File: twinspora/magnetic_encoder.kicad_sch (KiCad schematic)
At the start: 7 parts, among them J8 XY-SH1_0-6A51, U10 SRV05-4A, U8 MT6701QT

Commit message: NEW
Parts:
- C33: footprint Basic_Capacitors_Resistors:C0402 -> Capacitor_SMD:C_0402_1005Metric
- R26, R28, R30: footprint Basic_Capacitors_Resistors:R0603 -> Resistor_SMD:R_0603_1608Metric
- U10: footprint Package_TO_SOT_SMD:SOT-23-6 -> lemon-pepper-footprints:SOT-23-6
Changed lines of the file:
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@@
 		)
 	)
-	(text_box "SH breakouts for remote motor encoder connection (Must remove existing sensor)"
+	(text_box "SH breakouts for remote motor encoder connection (Desolder 0603 0Ω resistors)"
 		(exclude_from_sim no)
-		(at 182.88 66.04 0)
-		(size 26.67 13.3968)
+		(at 181.61 70.4232 0)
+		(size 24.13 9.5868)
 		(margins 0.9525 0.9525 0.9525 0.9525)
 		(stroke
@@
 		(dnp no)
 		(fields_autoplaced yes)
-		(property "Reference" "#PWR075"
+		(property "Reference" "#PWR75"
 			(at 173.99 81.28 0)
 			(hide yes)
@@
 			(project "twinspora"
 				(path "/64e594d2-0aaa-4fb1-a4b5-254d61e53018/0c28785f-fbfa-498f-abec-3f4cc9ccf6c4"
-					(reference "#PWR076")
+					(reference "#PWR76")
 					(unit 1)
 				)
 				(path "/64e594d2-0aaa-4fb1-a4b5-254d61e53018/59ac2ac7-da91-4c77-8dbc-3d7c7b498637"
-					(reference "#PWR075")
+					(reference "#PWR75")
 					(unit 1)
 				)
@@
 			)
 		)
-		(property "Footprint" "Basic_Capacitors_Resistors:R0603"
+		(property "Footprint" "Resistor_SMD:R_0603_1608Metric"
 			(at 115.57 102.87 0)
 			(hide yes)
@@
 		(dnp no)
 		(fields_autoplaced yes)
-		(property "Reference" "#PWR073"
+		(property "Reference" "#PWR73"
 			(at 215.9 81.28 0)
 			(hide yes)
@@
 			(project "twinspora"
 				(path "/64e594d2-0aaa-4fb1-a4b5-254d61e53018/0c28785f-fbfa-498f-abec-3f4cc9ccf6c4"
-					(reference "#PWR078")
+					(reference "#PWR78")
 					(unit 1)
 				)
 				(path "/64e594d2-0aaa-4fb1-a4b5-254d61e53018/59ac2ac7-da91-4c77-8dbc-3d7c7b498637"
-					(reference "#PWR073")
+					(reference "#PWR73")
 					(unit 1)
 				)
@@
 		(dnp no)
 		(fields_autoplaced yes)
-		(property "Reference" "#PWR074"
+		(property "Reference" "#PWR74"
 			(at 176.53 130.81 0)
 			(hide yes)
@@
 			(project "twinspora"
 				(path "/64e594d2-0aaa-4fb1-a4b5-254d61e53018/0c28785f-fbfa-498f-abec-3f4cc9ccf6c4"
-					(reference "#PWR077")
+					(reference "#PWR77")
 					(unit 1)
 				)
 				(path "/64e594d2-0aaa-4fb1-a4b5-254d61e53018/59ac2ac7-da91-4c77-8dbc-3d7c7b498637"
-					(reference "#PWR074")
+					(reference "#PWR74")
 					(unit 1)
 				)
@@
 		(dnp no)
 		(property "Reference" "C33"
-			(at 152.654 110.49 0)
+			(at 156.21 110.49 0)
 			(show_name no)
 			(do_not_autoplace no)
@@
 			)
 		)
-		(property "Footprint" "Basic_Capacitors_Resistors:C0402"
+		(property "Footprint" "Capacitor_SMD:C_0402_1005Metric"
 			(at 167.64 110.49 0)
 			(hide yes)
@@
 			)
 		)
-		(property "Footprint" "Basic_Capacitors_Resistors:R0603"
+		(property "Footprint" "Resistor_SMD:R_0603_1608Metric"
 			(at 107.95 100.33 0)
 			(hide yes)
@@
 		(dnp no)
 		(fields_autoplaced yes)
-		(property "Reference" "#PWR048"
+		(property "Reference" "#PWR48"
 			(at 140.97 81.28 0)
 			(hide yes)
@@
 			(project "twinspora"
 				(path "/64e594d2-0aaa-4fb1-a4b5-254d61e53018/0c28785f-fbfa-498f-abec-3f4cc9ccf6c4"
-					(reference "#PWR049")
+					(reference "#PWR49")
 					(unit 1)
 				)
 				(path "/64e594d2-0aaa-4fb1-a4b5-254d61e53018/59ac2ac7-da91-4c77-8dbc-3d7c7b498637"
-					(reference "#PWR048")
+					(reference "#PWR48")
 					(unit 1)
 				)
@@
 		(dnp no)
 		(property "Reference" "J8"
-			(at 190.5 101.5999 0)
-			(show_name no)
-			(do_not_autoplace no)
-			(effects
-				(font
-					(size 1.27 1.27)
-				)
-				(justify left)
+			(at 182.118 91.44 0)
+			(show_name no)
+			(do_not_autoplace no)
+			(effects
+				(font
+					(size 1.27 1.27)
+				)
 			)
 		)
 		(property "Value" "XY-SH1_0-6A51"
-			(at 184.15 104.14 0)
+			(at 196.342 118.618 0)
 			(hide yes)
 			(show_name no)
@@
 		(dnp no)
 		(fields_autoplaced yes)
-		(property "Reference" "#PWR051"
+		(property "Reference" "#PWR51"
 			(at 140.97 130.81 0)
 			(hide yes)
@@
 			(project "twinspora"
 				(path "/64e594d2-0aaa-4fb1-a4b5-254d61e53018/0c28785f-fbfa-498f-abec-3f4cc9ccf6c4"
-					(reference "#PWR052")
+					(reference "#PWR52")
 					(unit 1)
 				)
 				(path "/64e594d2-0aaa-4fb1-a4b5-254d61e53018/59ac2ac7-da91-4c77-8dbc-3d7c7b498637"
-					(reference "#PWR051")
+					(reference "#PWR51")
 					(unit 1)
 				)
@@
 			)
 		)
-		(property "Footprint" "Basic_Capacitors_Resistors:R0603"
+		(property "Footprint" "Resistor_SMD:R_0603_1608Metric"
 			(at 123.19 105.41 0)
 			(hide yes)
@@
 		(dnp no)
 		(property "Reference" "U10"
-			(at 219.0181 87.63 0)
+			(at 219.0497 87.63 0)
 			(show_name no)
 			(do_not_autoplace no)
@@
 		)
 		(property "Value" "SRV05-4A"
-			(at 219.0181 90.17 0)
+			(at 219.0497 90.17 0)
 			(show_name no)
 			(do_not_autoplace no)
@@
 			)
 		)
-		(property "Footprint" "Package_TO_SOT_SMD:SOT-23-6"
+		(property "Footprint" "lemon-pepper-footprints:SOT-23-6"
 			(at 233.68 114.3 0)
 			(hide yes)
@@
 		(dnp no)
 		(fields_autoplaced yes)
-		(property "Reference" "#PWR072"
+		(property "Reference" "#PWR72"
 			(at 215.9 130.81 0)
 			(hide yes)
@@
 			(project "twinspora"
 				(path "/64e594d2-0aaa-4fb1-a4b5-254d61e53018/0c28785f-fbfa-498f-abec-3f4cc9ccf6c4"
-					(reference "#PWR079")
+					(reference "#PWR79")
 					(unit 1)
 				)
 				(path "/64e594d2-0aaa-4fb1-a4b5-254d61e53018/59ac2ac7-da91-4c77-8dbc-3d7c7b498637"
-					(reference "#PWR072")
-					(unit 1)
-				)
+					(reference "#PWR72")
+					(unit 1)
+				)

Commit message: fix shit
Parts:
- U10: footprint lemon-pepper-footprints:SOT-23-6 -> Diode:SOT-23-6
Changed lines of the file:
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@@
 			)
 		)
-		(property "Footprint" "lemon-pepper-footprints:SOT-23-6"
+		(property "Footprint" "Diode:SOT-23-6"
 			(at 233.68 114.3 0)
 			(hide yes)

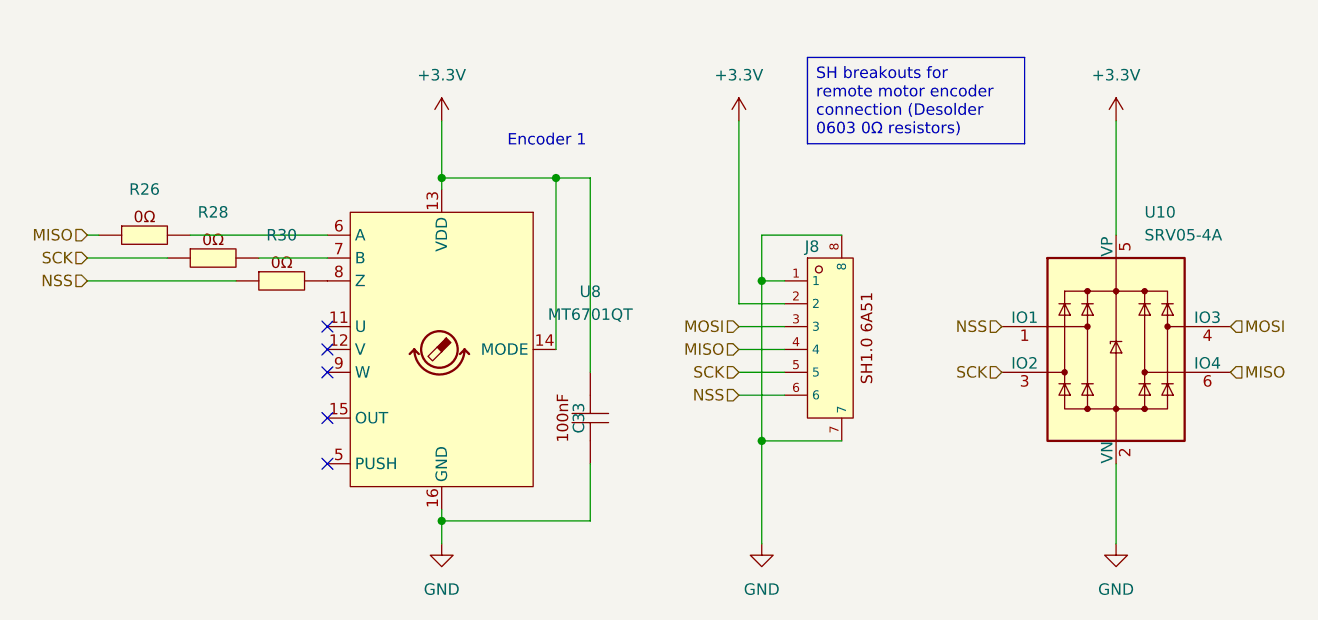
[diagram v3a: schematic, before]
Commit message: split terminatino for can
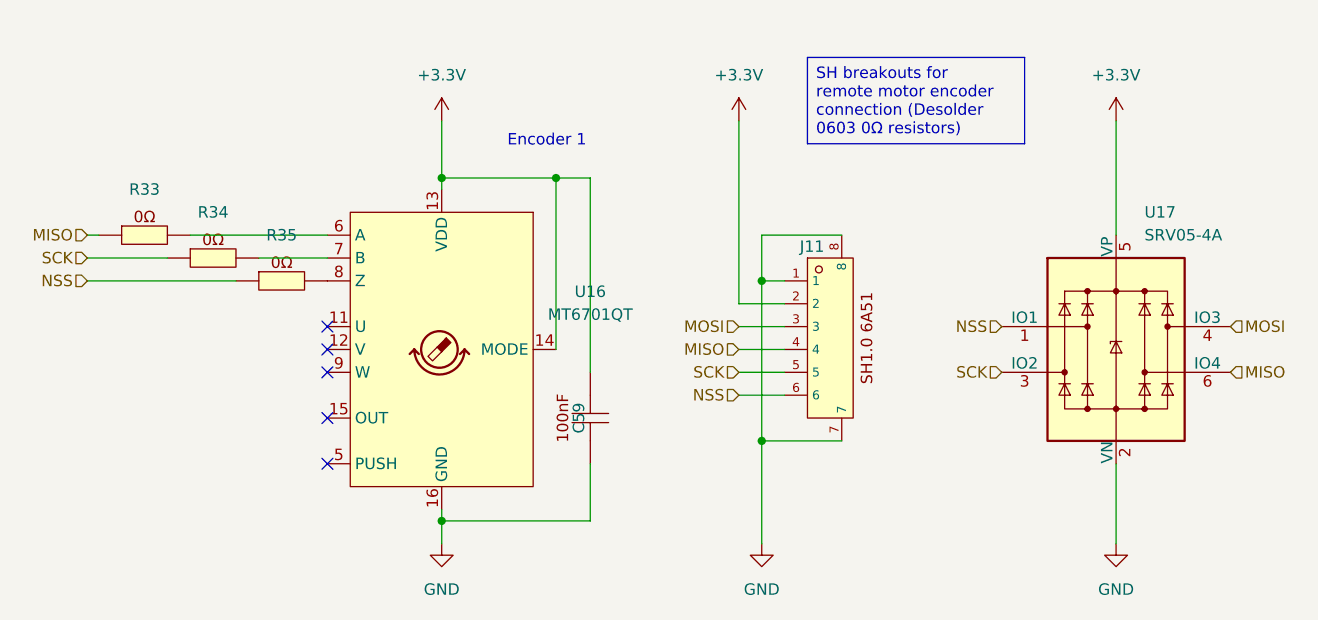
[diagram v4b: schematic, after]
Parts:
- renumbered C33 to C59, J8 to J11, R26 to R33, R28 to R34, R30 to R35, U8 to U16, U10 to U17
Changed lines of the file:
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@@
 		(dnp no)
 		(fields_autoplaced yes)
-		(property "Reference" "#PWR75"
+		(property "Reference" "#PWR084"
 			(at 173.99 81.28 0)
 			(hide yes)
@@
 			(project "twinspora"
 				(path "/64e594d2-0aaa-4fb1-a4b5-254d61e53018/0c28785f-fbfa-498f-abec-3f4cc9ccf6c4"
-					(reference "#PWR76")
+					(reference "#PWR090")
 					(unit 1)
 				)
 				(path "/64e594d2-0aaa-4fb1-a4b5-254d61e53018/59ac2ac7-da91-4c77-8dbc-3d7c7b498637"
-					(reference "#PWR75")
+					(reference "#PWR084")
 					(unit 1)
 				)
@@
 		(dnp no)
 		(fields_autoplaced yes)
-		(property "Reference" "R28"
+		(property "Reference" "R34"
 			(at 115.57 87.63 0)
 			(show_name no)
@@
 			(project "twinspora"
 				(path "/64e594d2-0aaa-4fb1-a4b5-254d61e53018/0c28785f-fbfa-498f-abec-3f4cc9ccf6c4"
-					(reference "R29")
+					(reference "R37")
 					(unit 1)
 				)
 				(path "/64e594d2-0aaa-4fb1-a4b5-254d61e53018/59ac2ac7-da91-4c77-8dbc-3d7c7b498637"
-					(reference "R28")
+					(reference "R34")
 					(unit 1)
 				)
@@
 		(dnp no)
 		(fields_autoplaced yes)
-		(property "Reference" "#PWR73"
+		(property "Reference" "#PWR086"
 			(at 215.9 81.28 0)
 			(hide yes)
@@
 			(project "twinspora"
 				(path "/64e594d2-0aaa-4fb1-a4b5-254d61e53018/0c28785f-fbfa-498f-abec-3f4cc9ccf6c4"
-					(reference "#PWR78")
+					(reference "#PWR092")
 					(unit 1)
 				)
 				(path "/64e594d2-0aaa-4fb1-a4b5-254d61e53018/59ac2ac7-da91-4c77-8dbc-3d7c7b498637"
-					(reference "#PWR73")
+					(reference "#PWR086")
 					(unit 1)
 				)
@@
 		(dnp no)
 		(fields_autoplaced yes)
-		(property "Reference" "#PWR74"
+		(property "Reference" "#PWR085"
 			(at 176.53 130.81 0)
 			(hide yes)
@@
 			(project "twinspora"
 				(path "/64e594d2-0aaa-4fb1-a4b5-254d61e53018/0c28785f-fbfa-498f-abec-3f4cc9ccf6c4"
-					(reference "#PWR77")
+					(reference "#PWR091")
 					(unit 1)
 				)
 				(path "/64e594d2-0aaa-4fb1-a4b5-254d61e53018/59ac2ac7-da91-4c77-8dbc-3d7c7b498637"
-					(reference "#PWR74")
+					(reference "#PWR085")
 					(unit 1)
 				)
@@
 		(in_pos_files yes)
 		(dnp no)
-		(property "Reference" "C33"
+		(property "Reference" "C59"
 			(at 156.21 110.49 0)
 			(show_name no)
@@
 			(project "twinspora"
 				(path "/64e594d2-0aaa-4fb1-a4b5-254d61e53018/0c28785f-fbfa-498f-abec-3f4cc9ccf6c4"
-					(reference "C34")
+					(reference "C60")
 					(unit 1)
 				)
 				(path "/64e594d2-0aaa-4fb1-a4b5-254d61e53018/59ac2ac7-da91-4c77-8dbc-3d7c7b498637"
-					(reference "C33")
+					(reference "C59")
 					(unit 1)
 				)
@@
 		(dnp no)
 		(fields_autoplaced yes)
-		(property "Reference" "R26"
+		(property "Reference" "R33"
 			(at 107.95 85.09 0)
 			(show_name no)
@@
 			(project "twinspora"
 				(path "/64e594d2-0aaa-4fb1-a4b5-254d61e53018/0c28785f-fbfa-498f-abec-3f4cc9ccf6c4"
-					(reference "R27")
+					(reference "R36")
 					(unit 1)
 				)
 				(path "/64e594d2-0aaa-4fb1-a4b5-254d61e53018/59ac2ac7-da91-4c77-8dbc-3d7c7b498637"
-					(reference "R26")
+					(reference "R33")
 					(unit 1)
 				)
@@
 		(dnp no)
 		(fields_autoplaced yes)
-		(property "Reference" "#PWR48"
+		(property "Reference" "#PWR082"
 			(at 140.97 81.28 0)
 			(hide yes)
@@
 			(project "twinspora"
 				(path "/64e594d2-0aaa-4fb1-a4b5-254d61e53018/0c28785f-fbfa-498f-abec-3f4cc9ccf6c4"
-					(reference "#PWR49")
+					(reference "#PWR088")
 					(unit 1)
 				)
 				(path "/64e594d2-0aaa-4fb1-a4b5-254d61e53018/59ac2ac7-da91-4c77-8dbc-3d7c7b498637"
-					(reference "#PWR48")
+					(reference "#PWR082")
 					(unit 1)
 				)
@@
 		(in_pos_files yes)
 		(dnp no)
-		(property "Reference" "J8"
+		(property "Reference" "J11"
 			(at 182.118 91.44 0)
 			(show_name no)
@@
 			(project "twinspora"
 				(path "/64e594d2-0aaa-4fb1-a4b5-254d61e53018/0c28785f-fbfa-498f-abec-3f4cc9ccf6c4"
-					(reference "J9")
+					(reference "J12")
 					(unit 1)
 				)
 				(path "/64e594d2-0aaa-4fb1-a4b5-254d61e53018/59ac2ac7-da91-4c77-8dbc-3d7c7b498637"
-					(reference "J8")
+					(reference "J11")
 					(unit 1)
 				)
@@
 		(dnp no)
 		(fields_autoplaced yes)
-		(property "Reference" "#PWR51"
+		(property "Reference" "#PWR083"
 			(at 140.97 130.81 0)
 			(hide yes)
@@
 			(project "twinspora"
 				(path "/64e594d2-0aaa-4fb1-a4b5-254d61e53018/0c28785f-fbfa-498f-abec-3f4cc9ccf6c4"
-					(reference "#PWR52")
+					(reference "#PWR089")
 					(unit 1)
 				)
 				(path "/64e594d2-0aaa-4fb1-a4b5-254d61e53018/59ac2ac7-da91-4c77-8dbc-3d7c7b498637"
-					(reference "#PWR51")
+					(reference "#PWR083")
 					(unit 1)
 				)
@@
 		(dnp no)
 		(fields_autoplaced yes)
-		(property "Reference" "R30"
+		(property "Reference" "R35"
 			(at 123.19 90.17 0)
 			(show_name no)
@@
 			(project "twinspora"
 				(path "/64e594d2-0aaa-4fb1-a4b5-254d61e53018/0c28785f-fbfa-498f-abec-3f4cc9ccf6c4"
-					(reference "R31")
+					(reference "R38")
 					(unit 1)
 				)
 				(path "/64e594d2-0aaa-4fb1-a4b5-254d61e53018/59ac2ac7-da91-4c77-8dbc-3d7c7b498637"
-					(reference "R30")
+					(reference "R35")
 					(unit 1)
 				)
@@
 		(dnp no)
 		(fields_autoplaced yes)
-		(property "Reference" "U8"
+		(property "Reference" "U16"
 			(at 157.48 96.4498 0)
 			(show_name no)
@@
 			(project "twinspora"
 				(path "/64e594d2-0aaa-4fb1-a4b5-254d61e53018/0c28785f-fbfa-498f-abec-3f4cc9ccf6c4"
-					(reference "U9")
+					(reference "U18")
 					(unit 1)
 				)
 				(path "/64e594d2-0aaa-4fb1-a4b5-254d61e53018/59ac2ac7-da91-4c77-8dbc-3d7c7b498637"
-					(reference "U8")
+					(reference "U16")
 					(unit 1)
 				)
@@
 		(in_pos_files yes)
 		(dnp no)
-		(property "Reference" "U10"
+		(property "Reference" "U17"
 			(at 219.0497 87.63 0)
 			(show_name no)
@@
 			(project "twinspora"
 				(path "/64e594d2-0aaa-4fb1-a4b5-254d61e53018/0c28785f-fbfa-498f-abec-3f4cc9ccf6c4"
-					(reference "U11")
+					(reference "U19")
 					(unit 1)
 				)
 				(path "/64e594d2-0aaa-4fb1-a4b5-254d61e53018/59ac2ac7-da91-4c77-8dbc-3d7c7b498637"
-					(reference "U10")
+					(reference "U17")
 					(unit 1)
 				)
@@
 		(dnp no)
 		(fields_autoplaced yes)
-		(property "Reference" "#PWR72"
+		(property "Reference" "#PWR087"
 			(at 215.9 130.81 0)
 			(hide yes)
@@
 			(project "twinspora"
 				(path "/64e594d2-0aaa-4fb1-a4b5-254d61e53018/0c28785f-fbfa-498f-abec-3f4cc9ccf6c4"
-					(reference "#PWR79")
+					(reference "#PWR093")
 					(unit 1)
 				)
 				(path "/64e594d2-0aaa-4fb1-a4b5-254d61e53018/59ac2ac7-da91-4c77-8dbc-3d7c7b498637"
-					(reference "#PWR72")
-					(unit 1)
-				)
+					(reference "#PWR087")
+					(unit 1)
+				)

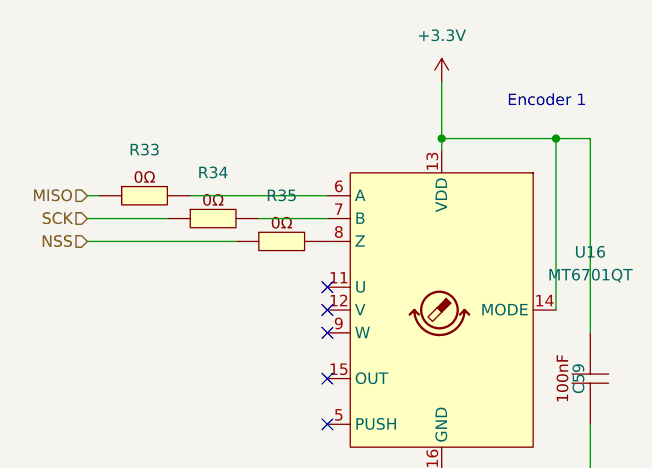
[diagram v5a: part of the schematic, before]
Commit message: fix silkscreen
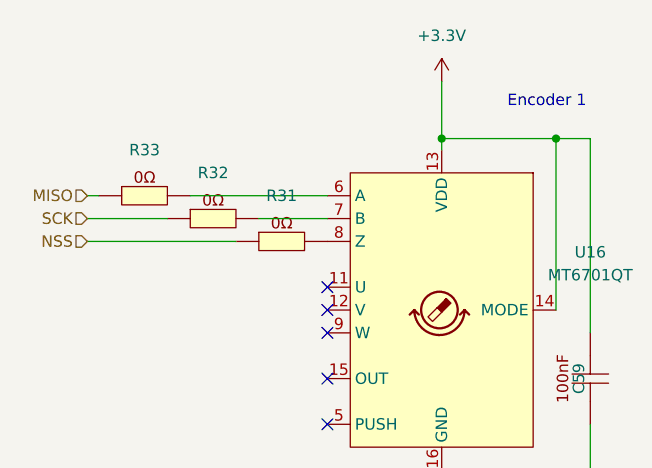
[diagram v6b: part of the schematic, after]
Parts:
- renumbered R35 to R31, R34 to R32
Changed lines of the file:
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@@
 		(dnp no)
 		(fields_autoplaced yes)
-		(property "Reference" "R34"
+		(property "Reference" "R32"
 			(at 115.57 87.63 0)
 			(show_name no)
@@
 				)
 				(path "/64e594d2-0aaa-4fb1-a4b5-254d61e53018/59ac2ac7-da91-4c77-8dbc-3d7c7b498637"
-					(reference "R34")
+					(reference "R32")
 					(unit 1)
 				)
@@
 		(dnp no)
 		(fields_autoplaced yes)
-		(property "Reference" "R35"
+		(property "Reference" "R31"
 			(at 123.19 90.17 0)
 			(show_name no)
@@
 				)
 				(path "/64e594d2-0aaa-4fb1-a4b5-254d61e53018/59ac2ac7-da91-4c77-8dbc-3d7c7b498637"
-					(reference "R35")
-					(unit 1)
-				)
+					(reference "R31")
+					(unit 1)
+				)
